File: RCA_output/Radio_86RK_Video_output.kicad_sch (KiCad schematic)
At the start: 10 parts, among them J1 VIDEO_OUT, J2 Conn_01x04_Pin, Q1 2N3904

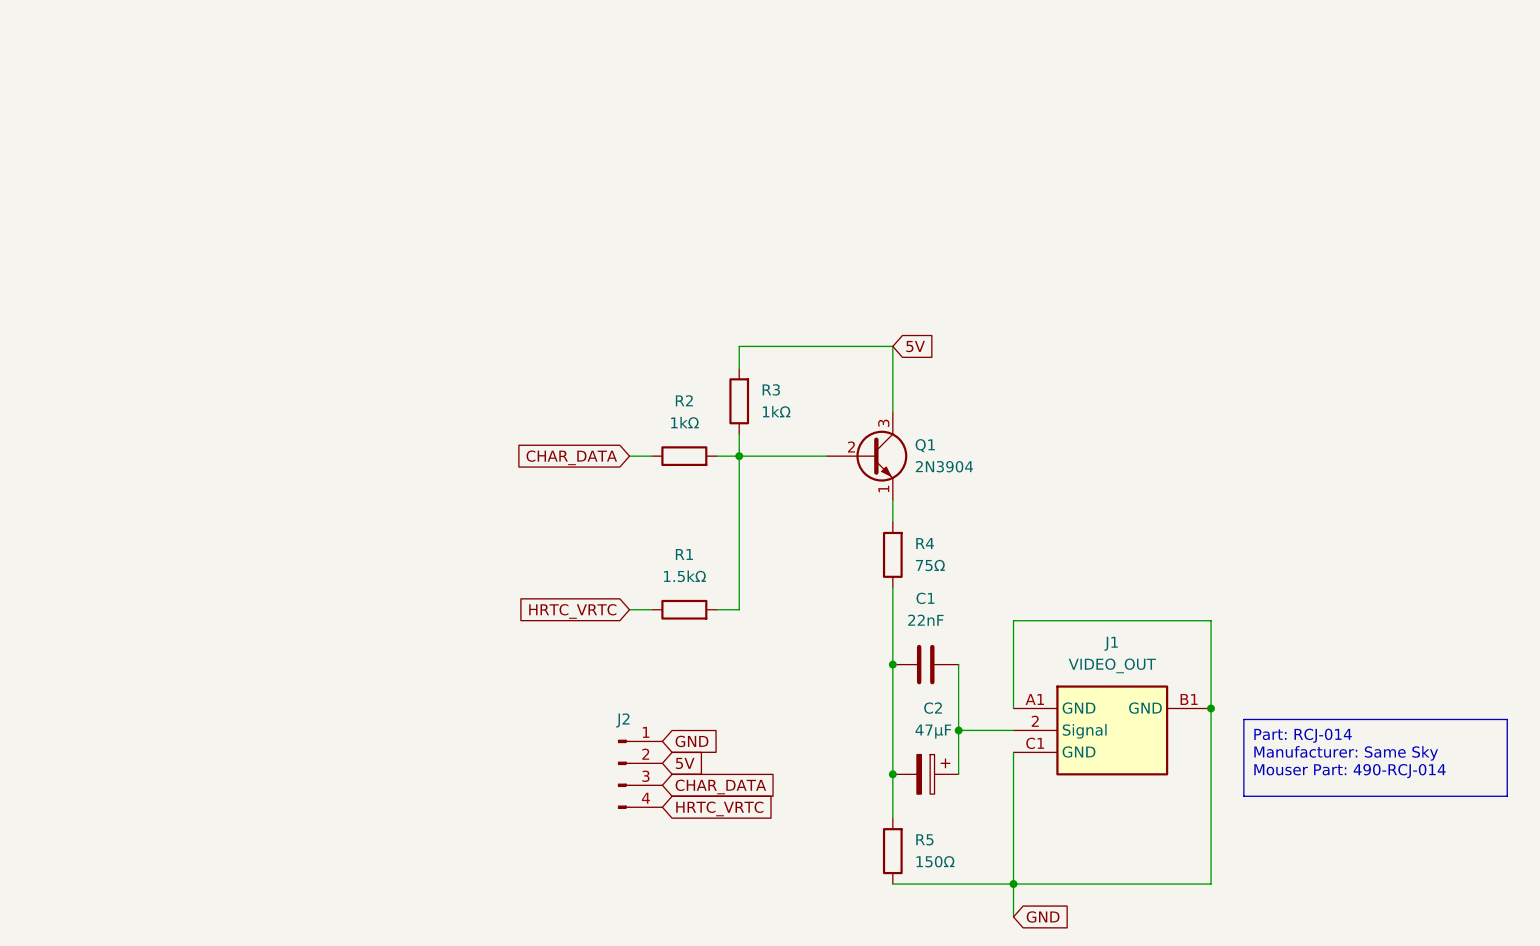
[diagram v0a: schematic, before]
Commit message: Added mounting hole
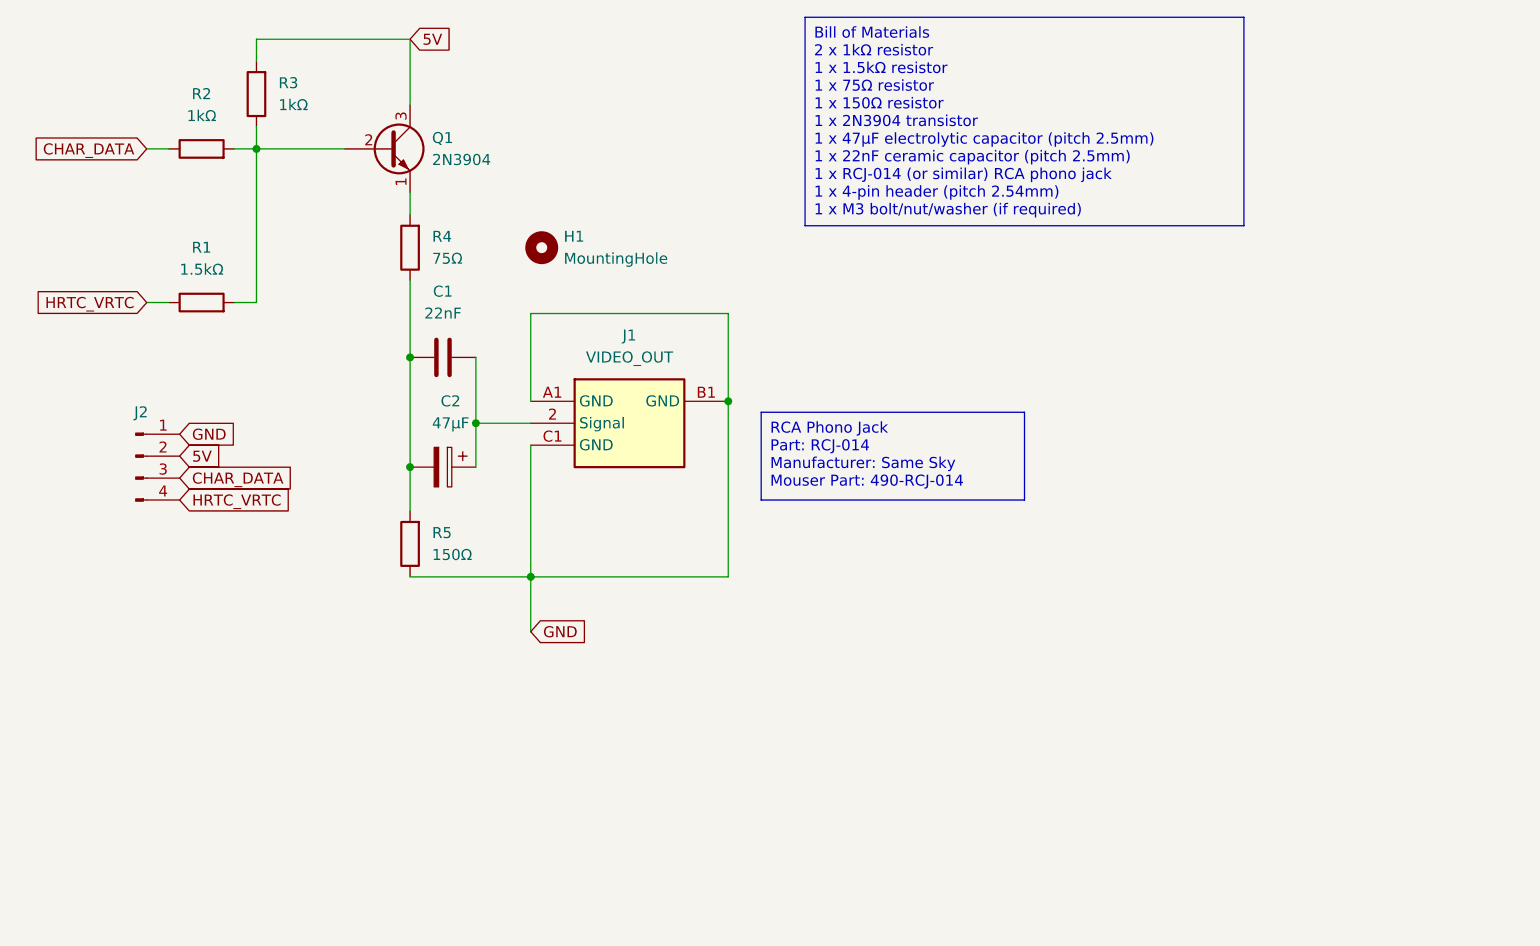
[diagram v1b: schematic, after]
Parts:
- added H1: MountingHole, MountingHole:MountingHole_3.2mm_M3, symbol Mechanical:MountingHole
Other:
- moved on the sheet: C1, C2, J1, J2, Q1, R1, R2, R3, R4, R5
